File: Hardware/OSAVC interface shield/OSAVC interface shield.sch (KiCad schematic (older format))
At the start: 34 parts, among them J1 DIGITAL, J11 I2C1, J12 GPS, J13 Radio, J14 RC RX, J2 COMMUNICATION, J20 Left Motor, J21 Right Motor, J22 Steering, J23 Encoder 4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

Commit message: fixed errors in layout
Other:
- note added: "1.1"
- note removed: "1"
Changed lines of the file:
@@
 March 4, 2021
 Text Notes 10600 7650 0    50   ~ 0
-1
+1.1
 Text Label 1800 5800 0    50   ~ 0
 GND

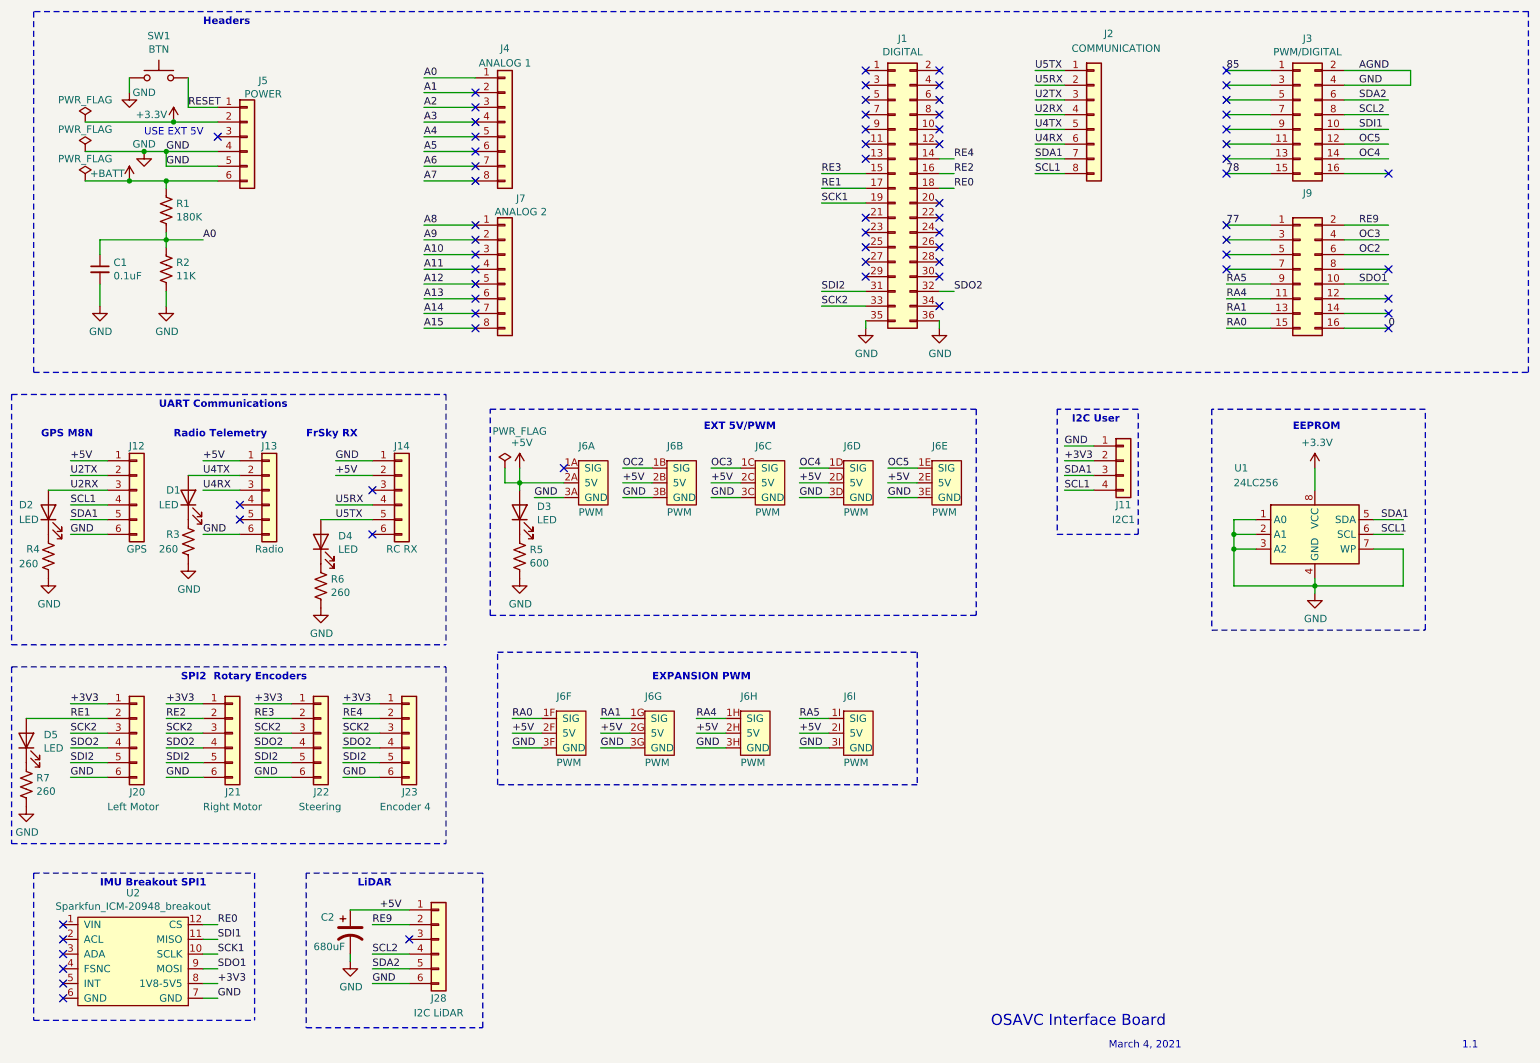
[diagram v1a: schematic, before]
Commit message: IMU: added high resolution message; I/O board:  minor fixes and added pullup resistors
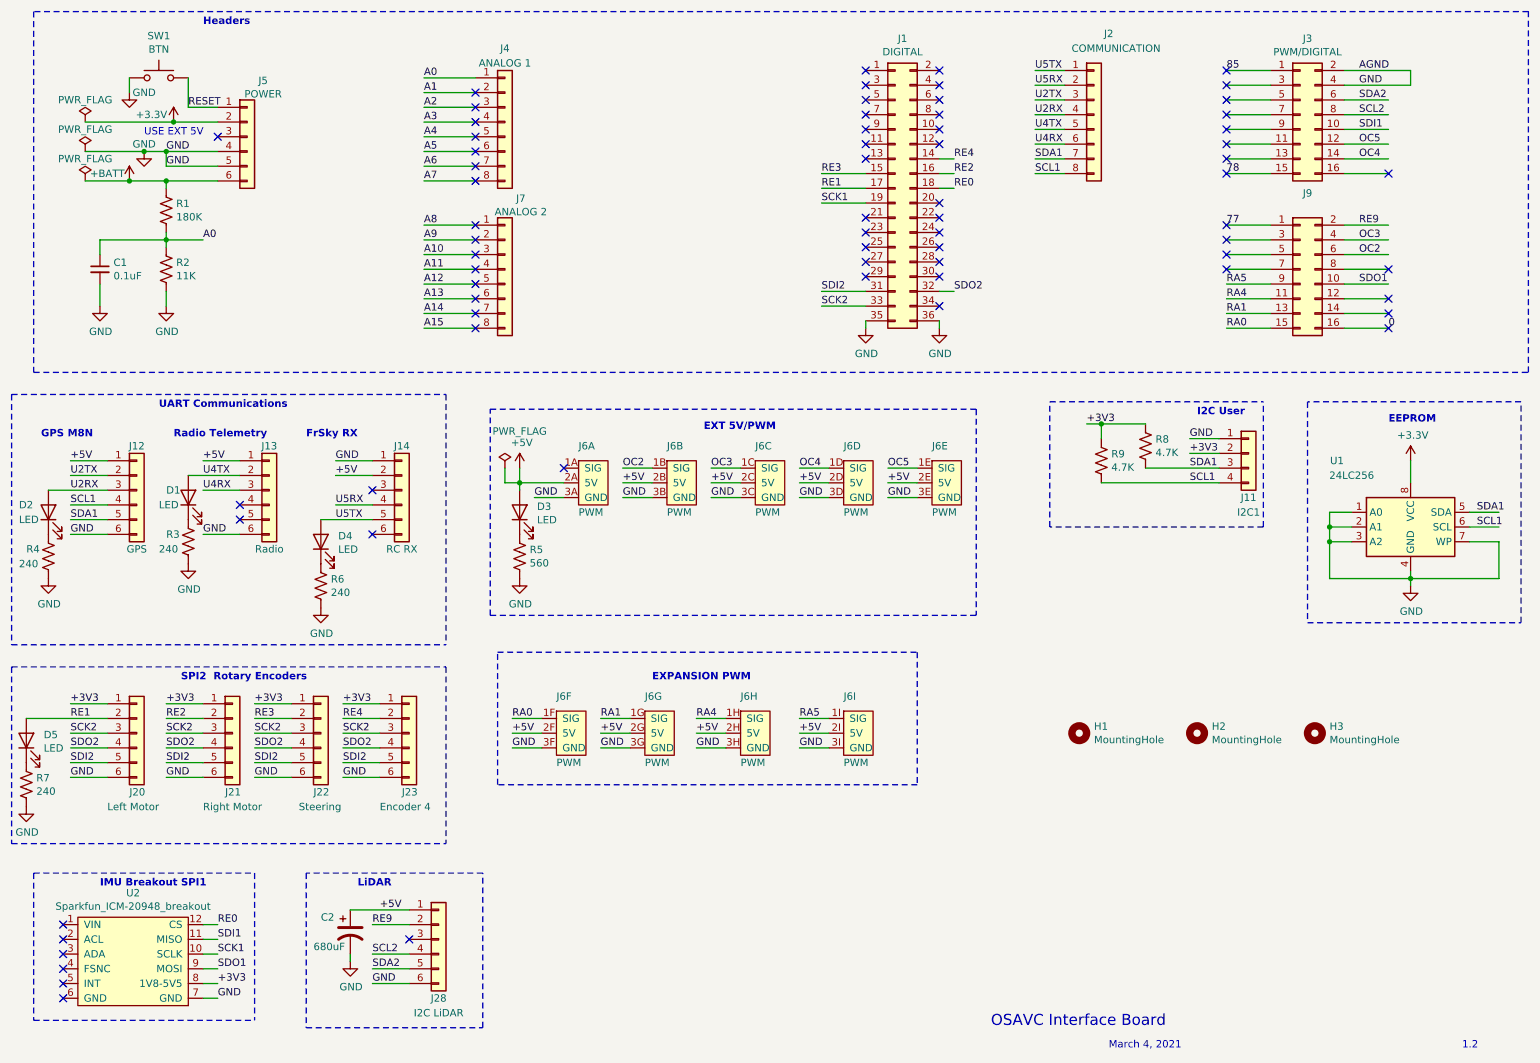
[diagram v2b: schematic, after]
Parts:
- added H1, H2, H3: MountingHole, MountingHole:MountingHole_3mm, symbol Mechanical:MountingHole
- added R8, R9: 4.7K, Resistor_SMD:R_0805_2012Metric, symbol Device:R_US
- R3, R4, R6, R7: value 260 -> 240
- R5: value 600 -> 560
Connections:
- wire segments 188 -> 191
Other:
- note added: "1.2"
- note removed: "1.1"
- moved on the sheet: J11, U1
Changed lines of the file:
@@
 Wire Wire Line
 	6100 5500 6300 5500
-Wire Wire Line
-	6100 5600 6300 5600
 Text Label 6100 5600 0    50   ~ 0
 GND
@@
 Text Notes 3100 6550 0    50   ~ 10
 LiDAR
-$Comp
-L Connector_Generic:Conn_01x04 J11
-U 1 1 6095F2D3
-P 8300 3650
-F 0 "J11" H 8300 3350 50  0000 C CNN
-F 1 "I2C1" H 8300 3250 50  0000 C CNN
-F 2 "Connector_PinHeader_2.54mm:PinHeader_1x04_P2.54mm_Vertical" H 8300 3650 50  0001 C CNN
-F 3 "~" H 8300 3650 50  0001 C CNN
-	1    8300 3650
-	1    0    0    -1
-$EndComp
-Wire Wire Line
-	7900 3550 8100 3550
-Wire Wire Line
-	7900 3650 8100 3650
-Wire Wire Line
-	7900 3750 8100 3750
-Wire Wire Line
-	7900 3850 8100 3850
-Text Label 7900 3550 0    50   ~ 0
-GND
-Text Label 7900 3750 0    50   ~ 0
-SDA1
-Text Label 7900 3850 0    50   ~ 0
-SCL1
-Text Notes 7950 3400 0    50   ~ 10
-I2C User
-Wire Notes Line
-	7850 4150 8400 4150
-Wire Notes Line
-	8400 4150 8400 3300
-Wire Notes Line
-	8400 3300 7850 3300
 NoConn ~ 3450 6900
 Text Label 3200 6800 0    50   ~ 0
@@
 Text Label 6100 5400 0    50   ~ 0
 RA5
-$Comp
-L Memory_EEPROM:24LC256 U1
-U 1 1 60A22AB4
-P 9600 4150
-F 0 "U1" H 9100 4600 50  0000 C CNN
-F 1 "24LC256" H 9200 4500 50  0000 C CNN
-F 2 "Package_SO:SOIJ-8_5.3x5.3mm_P1.27mm" H 9600 4150 50  0001 C CNN
-F 3 "http://ww1.microchip.com/downloads/en/devicedoc/21203m.pdf" H 9600 4150 50  0001 C CNN
-	1    9600 4150
-	1    0    0    -1
-$EndComp
-Wire Wire Line
-	10000 4050 10200 4050
-Wire Wire Line
-	10000 4150 10200 4150
-$Comp
-L power:GND #PWR012
-U 1 1 60A6A00D
-P 9600 4550
-F 0 "#PWR012" H 9600 4300 50  0001 C CNN
-F 1 "GND" H 9605 4377 50  0000 C CNN
-F 2 "" H 9600 4550 50  0001 C CNN
-F 3 "" H 9600 4550 50  0001 C CNN
-	1    9600 4550
-	1    0    0    -1
-$EndComp
-Wire Wire Line
-	9600 4450 9600 4500
-Wire Wire Line
-	9200 4050 9050 4050
-Wire Wire Line
-	9200 4150 9050 4150
-Wire Wire Line
-	9200 4250 9050 4250
-Wire Wire Line
-	9050 4050 9050 4150
-Wire Wire Line
-	9050 4150 9050 4250
-Connection ~ 9050 4150
-Wire Wire Line
-	9050 4250 9050 4500
-Wire Wire Line
-	9050 4500 9600 4500
-Connection ~ 9050 4250
-Connection ~ 9600 4500
-Wire Wire Line
-	9600 4500 9600 4550
-Wire Wire Line
-	10000 4250 10200 4250
-Wire Wire Line
-	10200 4250 10200 4500
-Wire Wire Line
-	10200 4500 9600 4500
-Text Notes 9450 3450 0    50   ~ 10
-EEPROM
-Wire Notes Line
-	8900 3300 8900 4800
-Wire Notes Line
-	8900 4800 10350 4800
-Wire Notes Line
-	10350 4800 10350 3300
-Wire Notes Line
-	10350 3300 8900 3300
-Text Label 10050 4050 0    50   ~ 0
-SDA1
-Text Label 10050 4150 0    50   ~ 0
-SCL1
 Text Notes 7400 7500 0    75   ~ 0
 OSAVC Interface Board
@@
 March 4, 2021
 Text Notes 10600 7650 0    50   ~ 0
-1.1
+1.2
 Text Label 1800 5800 0    50   ~ 0
 GND
@@
 NoConn ~ 3900 2750
 $Comp
-L power:+3.3V #PWR08
-U 1 1 6047F27C
-P 9600 3700
-F 0 "#PWR08" H 9600 3550 50  0001 C CNN
-F 1 "+3.3V" H 9615 3873 50  0000 C CNN
-F 2 "" H 9600 3700 50  0001 C CNN
-F 3 "" H 9600 3700 50  0001 C CNN
-	1    9600 3700
-	1    0    0    -1
-$EndComp
-Wire Wire Line
-	9600 3700 9600 3850
-$Comp
 L power:+3.3V #PWR02
 U 1 1 6049791D
@@
 Text Label 3000 5300 0    50   ~ 0
 +3V3
-Text Label 7900 3650 0    50   ~ 0
-+3V3
 $Comp
 L power:+5V #PWR07
@@
 P 4200 4300
 F 0 "R5" H 4268 4346 50  0000 L CNN
-F 1 "600" H 4268 4255 50  0000 L CNN
+F 1 "560" H 4268 4255 50  0000 L CNN
 F 2 "Resistor_SMD:R_0805_2012Metric" V 4240 4290 50  0001 C CNN
 F 3 "~" H 4200 4300 50  0001 C CNN
@@
 P 2850 4500
 F 0 "R6" H 2918 4546 50  0000 L CNN
-F 1 "260" H 2918 4455 50  0000 L CNN
+F 1 "240" H 2918 4455 50  0000 L CNN
 F 2 "Resistor_SMD:R_0805_2012Metric" V 2890 4490 50  0001 C CNN
 F 3 "~" H 2850 4500 50  0001 C CNN
@@
 P 1000 4300
 F 0 "R4" H 850 4350 50  0000 L CNN
-F 1 "260" H 800 4250 50  0000 L CNN
+F 1 "240" H 800 4250 50  0000 L CNN
 F 2 "Resistor_SMD:R_0805_2012Metric" V 1040 4290 50  0001 C CNN
 F 3 "~" H 1000 4300 50  0001 C CNN
@@
 P 850 5850
 F 0 "R7" H 918 5896 50  0000 L CNN
-F 1 "260" H 918 5805 50  0000 L CNN
+F 1 "240" H 918 5805 50  0000 L CNN
 F 2 "Resistor_SMD:R_0805_2012Metric" V 890 5840 50  0001 C CNN
 F 3 "~" H 850 5850 50  0001 C CNN
@@
 P 1950 4200
 F 0 "R3" H 1800 4250 50  0000 L CNN
-F 1 "260" H 1750 4150 50  0000 L CNN
+F 1 "240" H 1750 4150 50  0000 L CNN
 F 2 "Resistor_SMD:R_0805_2012Metric" V 1990 4190 50  0001 C CNN
 F 3 "~" H 1950 4200 50  0001 C CNN
@@
 Wire Notes Line
 	750  6250 3700 6250
-Wire Notes Line
-	7850 3300 7850 4150
 Wire Wire Line
 	3050 7000 3050 7050
@@
 	1    0    0    -1
 $EndComp
+Wire Wire Line
+	6100 5600 6300 5600
+Text Label 8750 3600 0    50   ~ 0
++3V3
+Text Notes 8800 3350 0    50   ~ 10
+I2C User
+Text Label 8750 3800 0    50   ~ 0
+SCL1
+Text Label 8750 3700 0    50   ~ 0
+SDA1
+Text Label 8750 3500 0    50   ~ 0
+GND
+Wire Wire Line
+	8750 3600 8950 3600
+Wire Wire Line
+	8750 3500 8950 3500
+$Comp
+L Connector_Generic:Conn_01x04 J11
+U 1 1 6095F2D3
+P 9150 3600
+F 0 "J11" H 9150 3300 50  0000 C CNN
+F 1 "I2C1" H 9150 3200 50  0000 C CNN
+F 2 "Connector_PinHeader_2.54mm:PinHeader_1x04_P2.54mm_Vertical" H 9150 3600 50  0001 C CNN
+F 3 "~" H 9150 3600 50  0001 C CNN
+	1    9150 3600
+	1    0    0    -1
+$EndComp
+Wire Notes Line
+	9250 4100 9250 3250
+Wire Wire Line
+	10250 3650 10250 3800
+$Comp
+L power:+3.3V #PWR08
+U 1 1 6047F27C
+P 10250 3650
+F 0 "#PWR08" H 10250 3500 50  0001 C CNN
+F 1 "+3.3V" H 10265 3823 50  0000 C CNN
+F 2 "" H 10250 3650 50  0001 C CNN
+F 3 "" H 10250 3650 50  0001 C CNN
+	1    10250 3650
+	1    0    0    -1
+$EndComp
+Text Label 10700 4100 0    50   ~ 0
+SCL1
+Text Label 10700 4000 0    50   ~ 0
+SDA1
+Wire Notes Line
+	11000 3250 9550 3250
+Wire Notes Line
+	11000 4750 11000 3250
+Wire Notes Line
+	9550 4750 11000 4750
+Wire Notes Line
+	9550 3250 9550 4750
+Text Notes 10100 3400 0    50   ~ 10
+EEPROM
+Wire Wire Line
+	10850 4450 10250 4450
+Wire Wire Line
+	10850 4200 10850 4450
+Wire Wire Line
+	10650 4200 10850 4200
+Wire Wire Line
+	10250 4450 10250 4500
+Connection ~ 10250 4450
+Connection ~ 9700 4200
+Wire Wire Line
+	9700 4450 10250 4450
+Wire Wire Line
+	9700 4200 9700 4450
+Connection ~ 9700 4100
+Wire Wire Line
+	9700 4100 9700 4200
+Wire Wire Line
+	9700 4000 9700 4100
+Wire Wire Line
+	9850 4200 9700 4200
+Wire Wire Line
+	9850 4100 9700 4100
+Wire Wire Line
+	9850 4000 9700 4000
+Wire Wire Line
+	10250 4400 10250 4450
+$Comp
+L power:GND #PWR012
+U 1 1 60A6A00D
+P 10250 4500
+F 0 "#PWR012" H 10250 4250 50  0001 C CNN
+F 1 "GND" H 10255 4327 50  0000 C CNN
+F 2 "" H 10250 4500 50  0001 C CNN
+F 3 "" H 10250 4500 50  0001 C CNN
+	1    10250 4500
+	1    0    0    -1
+$EndComp
+Wire Wire Line
+	10650 4100 10850 4100
+Wire Wire Line
+	10650 4000 10850 4000
+$Comp
+L Memory_EEPROM:24LC256 U1
+U 1 1 60A22AB4
+P 10250 4100
+F 0 "U1" H 9750 4550 50  0000 C CNN
+F 1 "24LC256" H 9850 4450 50  0000 C CNN
+F 2 "Package_SO:SOIJ-8_5.3x5.3mm_P1.27mm" H 10250 4100 50  0001 C CNN
+F 3 "http://ww1.microchip.com/downloads/en/devicedoc/21203m.pdf" H 10250 4100 50  0001 C CNN
+	1    10250 4100
+	1    0    0    -1
+$EndComp
+$Comp
+L Device:R_US R9
+U 1 1 6108F527
+P 8150 3650
+F 0 "R9" H 8218 3696 50  0000 L CNN
+F 1 "4.7K" H 8218 3605 50  0000 L CNN
+F 2 "Resistor_SMD:R_0805_2012Metric" V 8190 3640 50  0001 C CNN
+F 3 "~" H 8150 3650 50  0001 C CNN
+	1    8150 3650
+	1    0    0    -1
+$EndComp
+$Comp
+L Device:R_US R8
+U 1 1 61090BDB
+P 8450 3550
+F 0 "R8" H 8518 3596 50  0000 L CNN
+F 1 "4.7K" H 8518 3505 50  0000 L CNN
+F 2 "Resistor_SMD:R_0805_2012Metric" V 8490 3540 50  0001 C CNN
+F 3 "~" H 8450 3550 50  0001 C CNN
+	1    8450 3550
+	1    0    0    -1
+$EndComp
+Wire Wire Line
+	8150 3800 8950 3800
+Wire Wire Line
+	8450 3700 8950 3700
+Wire Wire Line
+	8450 3400 8150 3400
+Wire Wire Line
+	8150 3500 8150 3400
+Connection ~ 8150 3400
+Wire Wire Line
+	8150 3400 8050 3400
+Text Label 8050 3400 0    50   ~ 0
++3V3
+Wire Notes Line
+	9250 4100 7800 4100
+Wire Notes Line
+	7800 4100 7800 3250
+Wire Notes Line
+	7800 3250 9250 3250
+$Comp
+L Mechanical:MountingHole H1
+U 1 1 61144D3C
+P 8000 5500
+F 0 "H1" H 8100 5546 50  0000 L CNN
+F 1 "MountingHole" H 8100 5455 50  0000 L CNN
+F 2 "MountingHole:MountingHole_3mm" H 8000 5500 50  0001 C CNN
+F 3 "~" H 8000 5500 50  0001 C CNN
+	1    8000 5500
+	1    0    0    -1
+$EndComp
+$Comp
+L Mechanical:MountingHole H2
+U 1 1 611457EF
+P 8800 5500
+F 0 "H2" H 8900 5546 50  0000 L CNN
+F 1 "MountingHole" H 8900 5455 50  0000 L CNN
+F 2 "MountingHole:MountingHole_3mm" H 8800 5500 50  0001 C CNN
+F 3 "~" H 8800 5500 50  0001 C CNN
+	1    8800 5500
+	1    0    0    -1
+$EndComp
+$Comp
+L Mechanical:MountingHole H3
+U 1 1 61146A75
+P 9600 5500
+F 0 "H3" H 9700 5546 50  0000 L CNN
+F 1 "MountingHole" H 9700 5455 50  0000 L CNN
+F 2 "MountingHole:MountingHole_3mm" H 9600 5500 50  0001 C CNN
+F 3 "~" H 9600 5500 50  0001 C CNN
+	1    9600 5500
+	1    0    0    -1
+$EndComp
